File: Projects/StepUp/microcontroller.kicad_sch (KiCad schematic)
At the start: 38 parts, among them J1 USB_C_Receptacle_USB2.0_16P, J2 Conn_01x02, J3 Conn_02x03_Counter_Clockwise, J4 Conn_02x05_Counter_Clockwise, SW1 SW_Push, SW2 SW_Push, SW3 SW_Push, U1 USBLC6-2SC6, U2 W25Q128JVS, U3 RP2040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

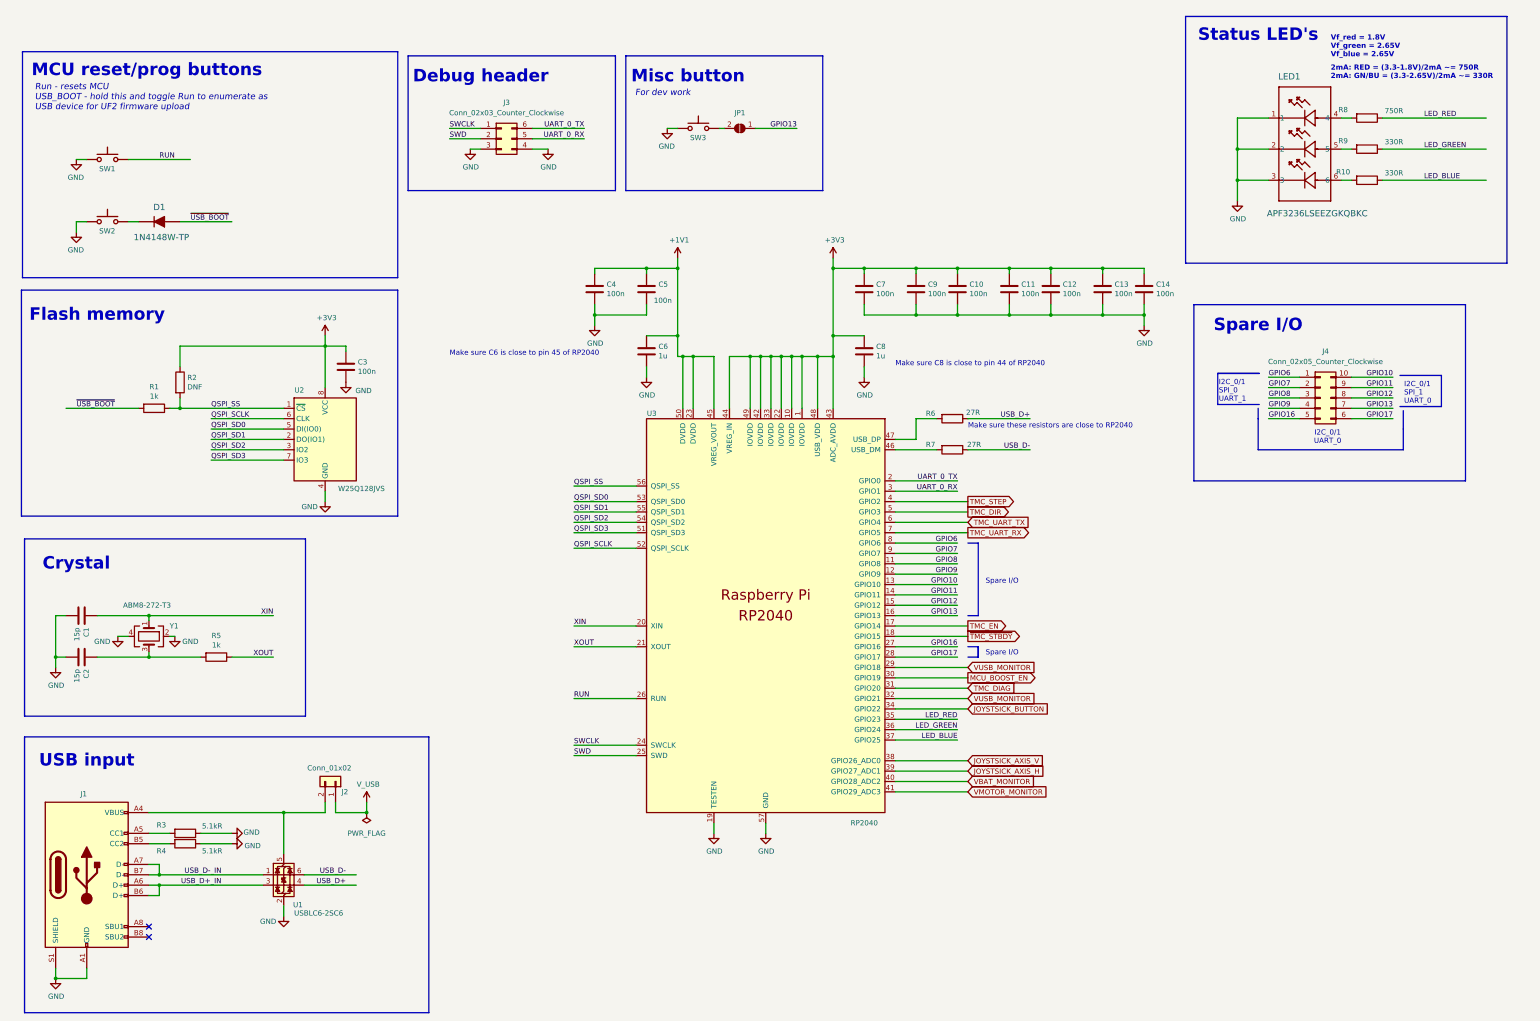
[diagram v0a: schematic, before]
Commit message: feat(tidy): Bigger PMOS, added footprints
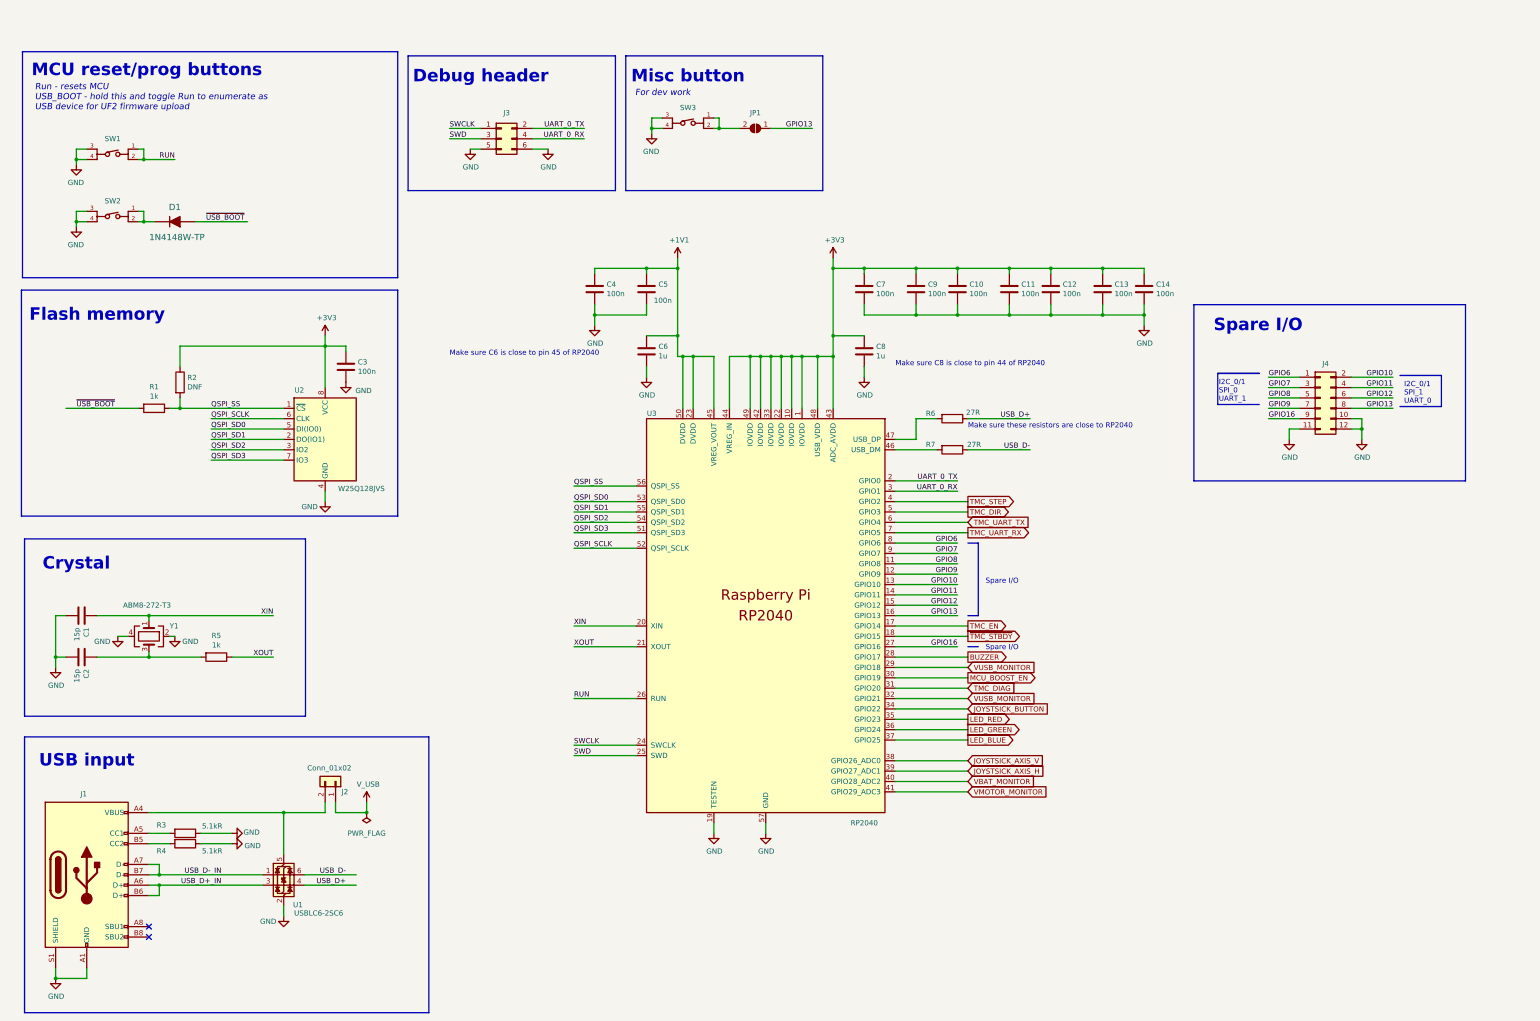
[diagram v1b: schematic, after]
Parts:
- removed J3: Conn_02x03_Counter_Clockwise, Connector_PinHeader_2.54mm:PinHeader_2x03_P2.54mm_Vertical, symbol Connector_Generic:Conn_02x03_Counter_Clockwise
- removed J4: Conn_02x05_Counter_Clockwise, Connector_PinHeader_2.54mm:PinHeader_2x05_P2.54mm_Vertical, symbol Connector_Generic:Conn_02x05_Counter_Clockwise
- removed LED1: APF3236LSEEZGKQBKC, Snapeda:APF3236LSEEZGKQBKC_KNB, symbol Snapeda_kicad_2:APF3236LSEEZGKQBKC
- removed R10, R9: 330R, Resistor_SMD:R_0603_1608Metric, symbol Device:R
- removed R8: 750R, Resistor_SMD:R_0603_1608Metric, symbol Device:R
- removed SW1, SW2, SW3: SW_Push, Button_Switch_SMD:SW_Push_1P1T_NO_Vertical_Wuerth_434133025816, symbol Switch:SW_Push
- added J3: Conn_02x03_Odd_Even, Connector_PinHeader_2.54mm:PinHeader_2x03_P2.54mm_Vertical, symbol Connector_Generic:Conn_02x03_Odd_Even
- added J4: Conn_02x06_Odd_Even, Connector_PinHeader_2.54mm:PinHeader_2x06_P2.54mm_Vertical, symbol Connector_Generic:Conn_02x06_Odd_Even
- added SW1, SW2, SW3: 434133025816, Snapeda:434133025816_434133025816, symbol Snapeda_kicad_2:434133025816
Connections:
- net GND: now also J3.5 (Pin_5), J3.6 (Pin_6), J4.10 (Pin_10), J4.11 (Pin_11), J4.12 (Pin_12), SW1.3, SW1.4, SW2.3, SW2.4, SW3.3, SW3.4
- net GPIO10: now also J4.2 (Pin_2)
- net GPIO11: now also J4.4 (Pin_4)
- net GPIO12: now also J4.6 (Pin_6)
- net GPIO13: now also J4.8 (Pin_8)
- net GPIO16: now also J4.9 (Pin_9)
- net GPIO6: now also J4.1 (Pin_1)
- net GPIO7: now also J4.3 (Pin_3)
- net GPIO8: now also J4.5 (Pin_5)
- net GPIO9: now also J4.7 (Pin_7)
- net RUN: now also SW1.1, SW1.2
- net SWCLK: now also J3.1 (Pin_1)
- net SWD: now also J3.3 (Pin_3)
- net UART_0_RX: now also J3.4 (Pin_4)
- net UART_0_TX: now also J3.2 (Pin_2)
- net at D1.K: now also SW2.1, SW2.2
- net at JP1.2 (B): now also SW3.1, SW3.2
- net GPIO17 renamed BUZZER
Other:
- note removed: "2mA: RED = (3.3-1.8V)/2mA ~= 750R 2mA: GN/BU = (3.3-2.65V)/2mA ~= 330R"
- note removed: "I2C_0/1 UART_0"
- note removed: "Status LED's"
- note removed: "Vf_red = 1.8V Vf_green = 2.65V Vf_blue = 2.65V"
- moved on the sheet: D1, JP1

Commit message: feat(layout): TMC & Boost layout begin
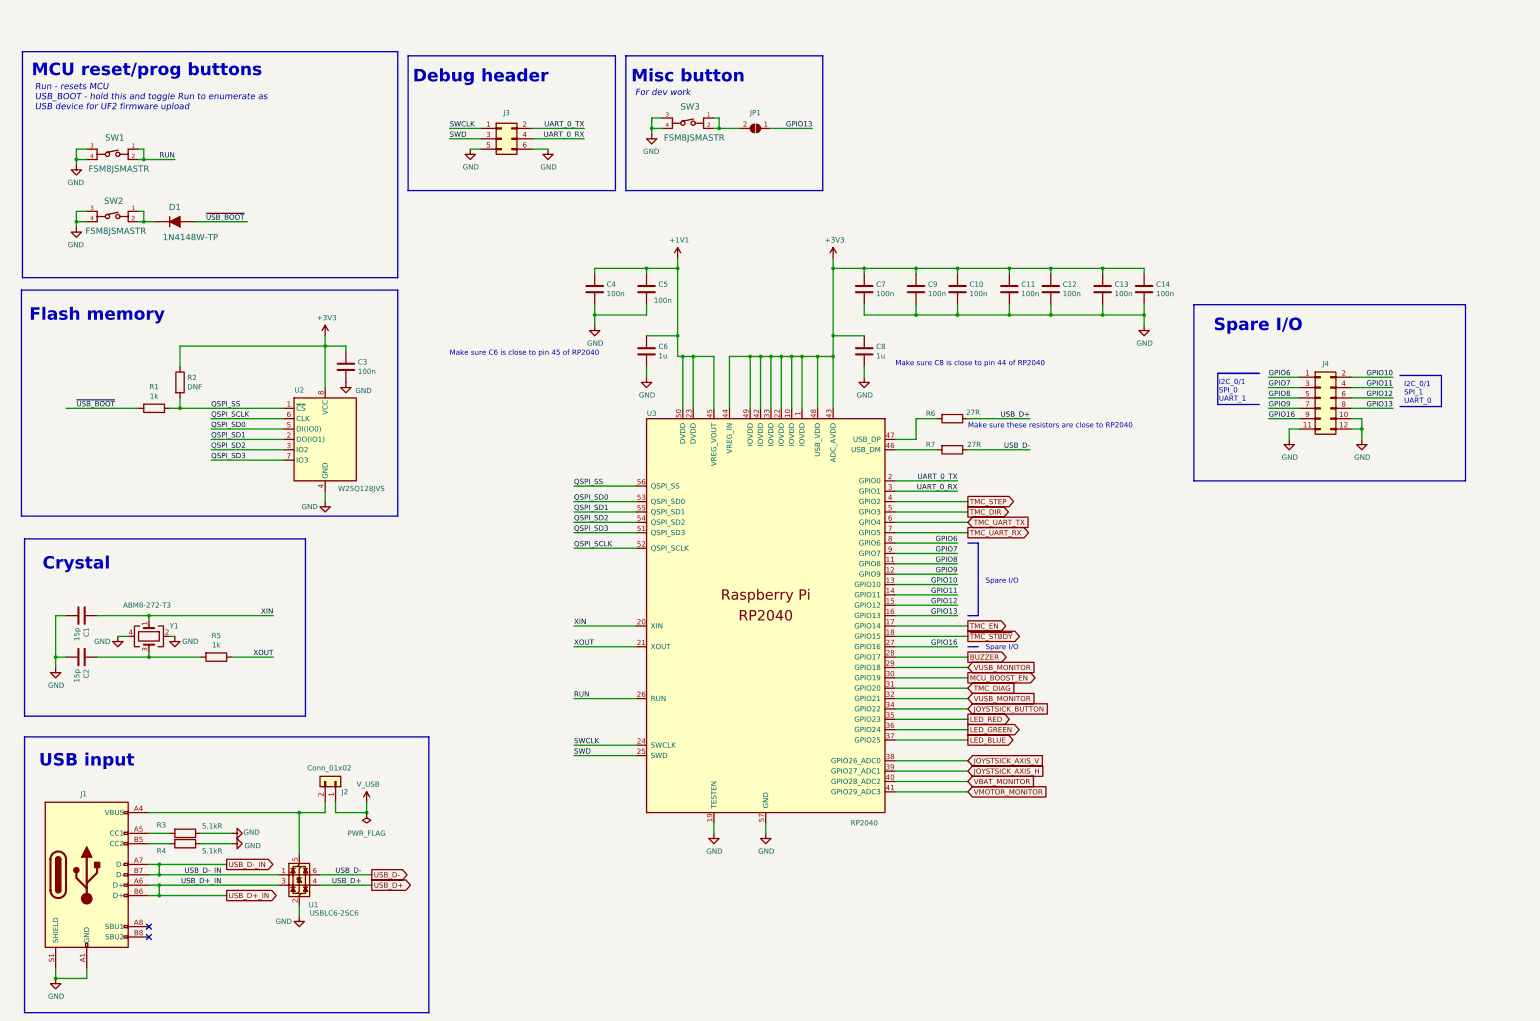
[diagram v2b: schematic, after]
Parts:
- removed SW1, SW2, SW3: 434133025816, Snapeda:434133025816_434133025816, symbol Snapeda_kicad_2:434133025816
- added SW1, SW2, SW3: FSM8JSMASTR, Snapeda:SW4_FSM8JSMASTR_TEC, symbol Snapeda_kicad_2:FSM8JSMASTR
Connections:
- net GND: now also SW1.3, SW1.4, SW2.3, SW2.4, SW3.3, SW3.4
- net RUN: now also SW1.1, SW1.2
- net at JP1.2 (B): now also SW3.1, SW3.2
- net at D1.K: now also SW2.1, SW2.2
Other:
- moved on the sheet: U1
